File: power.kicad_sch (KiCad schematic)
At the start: 41 parts, among them U2 BQ25176J, U3 TPS61201DRC, U4 BQ51050BRHL

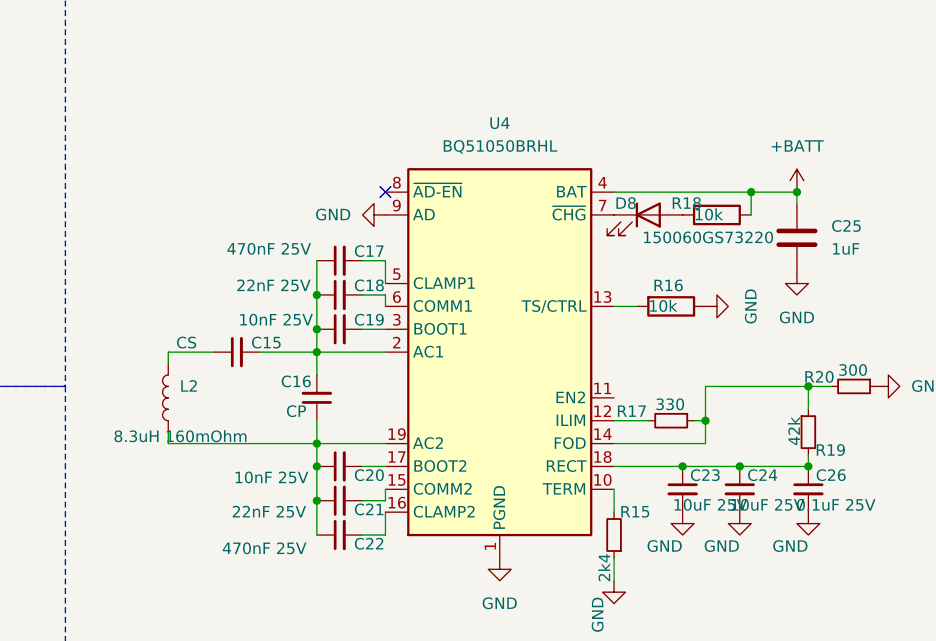
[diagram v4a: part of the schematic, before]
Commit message: start reshuffeling for qi-charge version
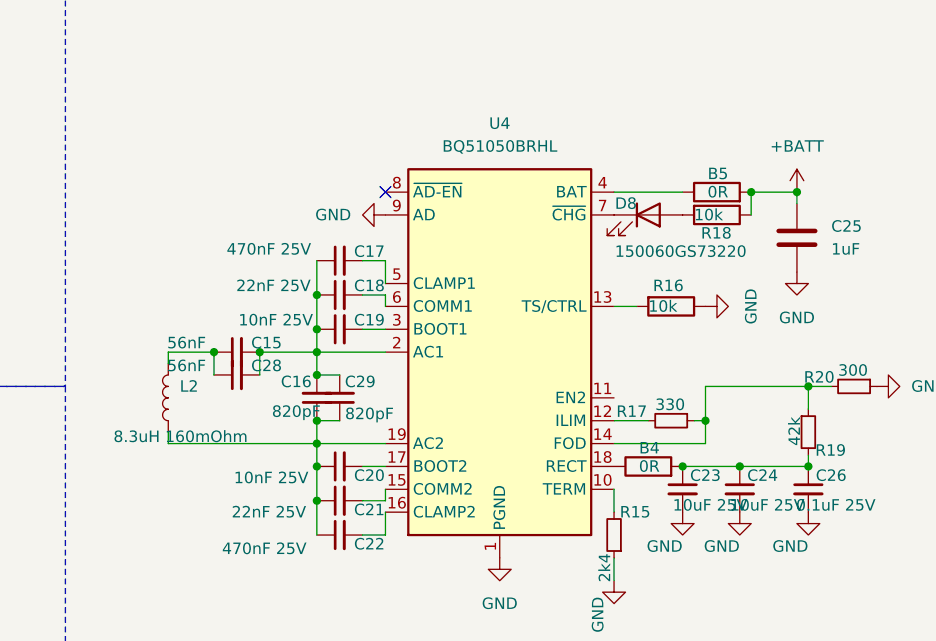
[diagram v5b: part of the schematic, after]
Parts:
- added B4, B5: 0R, Resistor_SMD:R_1206_3216Metric, symbol Device:R
- added C28: 56nF, Capacitor_SMD:C_0402_1005Metric, symbol Device:C_Small
- added C29: 820pF, Capacitor_SMD:C_0402_1005Metric, symbol Device:C_Small
- C15: value CS -> 56nF
- C16: value CP -> 820pF
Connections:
- net +BATT: now also B5.2; no longer U4.4 (BAT)
- net at C16.1, C20.1, C21.1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: now also C29.1
- net at C15.2, C16.2, C17.1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: now also C28.2, C29.2
- net at C23.1, C24.1, C26.1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: now also B4.2; no longer U4.18 (RECT)
- net at C15.1, L2.2: now also C28.1
- new net: B4.1, U4.18 (RECT)
- new net: B5.1, U4.4 (BAT)

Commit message: further work
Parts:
- C13: footprint Capacitor_SMD:C_0805_2012Metric -> Capacitor_SMD:C_0603_1608Metric
- R10, R11, R12, R13, R14, R16, R18, R8, R9: footprint Resistor_SMD:R_0805_2012Metric -> Resistor_SMD:R_0603_1608Metric
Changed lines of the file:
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@@
 			)
 		)
-		(property "Footprint" "Resistor_SMD:R_0805_2012Metric"
+		(property "Footprint" "Resistor_SMD:R_0603_1608Metric"
 			(at 218.44 68.072 90)
 			(effects
@@
 			)
 		)
-		(property "Footprint" "Resistor_SMD:R_0805_2012Metric"
+		(property "Footprint" "Resistor_SMD:R_0603_1608Metric"
 			(at 65.532 62.23 90)
 			(effects
@@
 			)
 		)
-		(property "Footprint" "Capacitor_SMD:C_0805_2012Metric"
+		(property "Footprint" "Capacitor_SMD:C_0603_1608Metric"
 			(at 107.6452 76.2 0)
 			(effects
@@
 			)
 		)
-		(property "Footprint" "Resistor_SMD:R_0805_2012Metric"
+		(property "Footprint" "Resistor_SMD:R_0603_1608Metric"
 			(at 86.36 129.032 90)
 			(effects
@@
 			)
 		)
-		(property "Footprint" "Resistor_SMD:R_0805_2012Metric"
+		(property "Footprint" "Resistor_SMD:R_0603_1608Metric"
 			(at 42.672 134.62 90)
 			(effects
@@
 			)
 		)
-		(property "Footprint" "Resistor_SMD:R_0805_2012Metric"
+		(property "Footprint" "Resistor_SMD:R_0603_1608Metric"
 			(at 79.248 140.97 90)
 			(effects
@@
 			)
 		)
-		(property "Footprint" "Resistor_SMD:R_0805_2012Metric"
+		(property "Footprint" "Resistor_SMD:R_0603_1608Metric"
 			(at 86.36 123.952 90)
 			(effects
@@
 			)
 		)
-		(property "Footprint" "Resistor_SMD:R_0805_2012Metric"
+		(property "Footprint" "Resistor_SMD:R_0603_1608Metric"
 			(at 213.36 78.232 90)
 			(effects
@@
 			)
 		)
-		(property "Footprint" "Resistor_SMD:R_0805_2012Metric"
+		(property "Footprint" "Resistor_SMD:R_0603_1608Metric"
 			(at 49.022 138.43 90)
 			(effects
@@
 			)
 		)
-		(property "Footprint" "Resistor_SMD:R_0805_2012Metric"
+		(property "Footprint" "Resistor_SMD:R_0603_1608Metric"
 			(at 65.532 76.2 90)
 			(effects

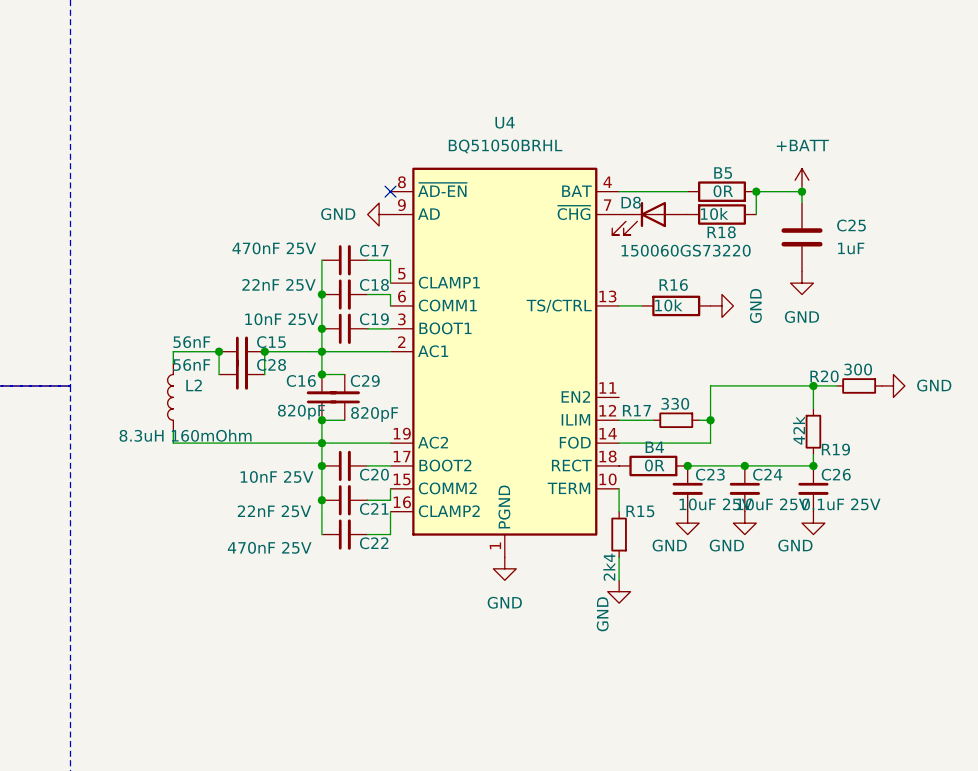
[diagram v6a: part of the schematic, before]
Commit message: add usb c connector
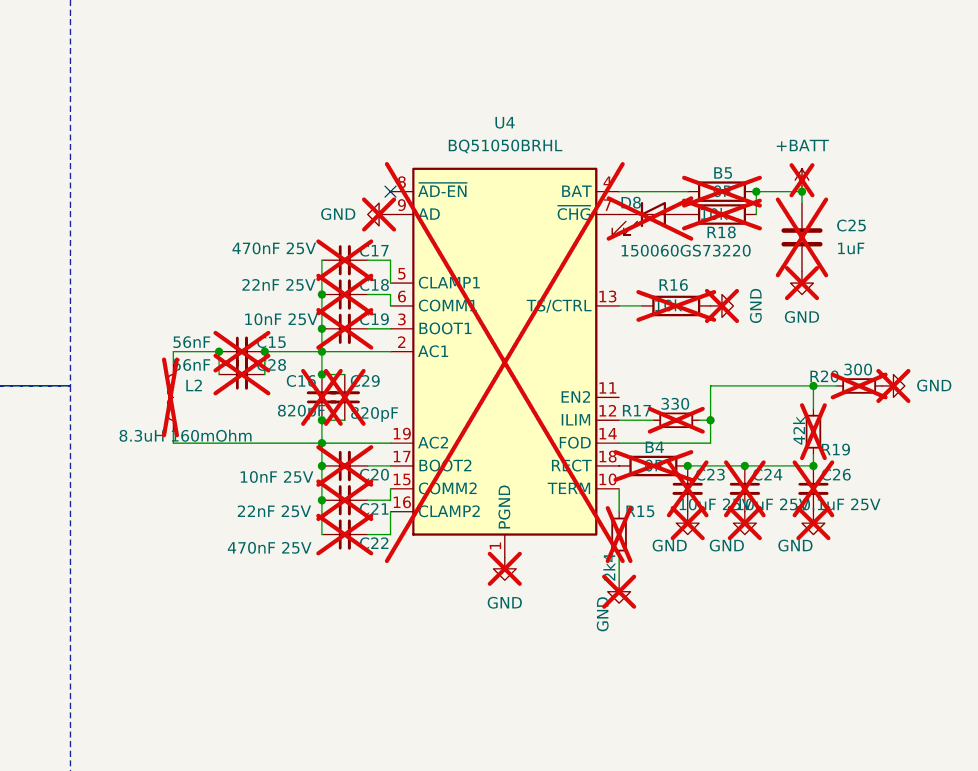
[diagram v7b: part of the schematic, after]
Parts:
- B4, B5, C15, C16, C17, C18, C19, C20, C21, C22, C23, C24, C25, C26, C28, C29, D8, L2, R15, R16, R17, R18, R19, R20, U4: now not fitted; now left out of the parts list
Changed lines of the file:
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@@
 		(unit 1)
 		(exclude_from_sim no)
-		(in_bom yes)
-		(on_board yes)
-		(dnp no)
+		(in_bom no)
+		(on_board no)
+		(dnp yes)
 		(property "Reference" "R18"
 			(at 216.662 71.882 90)
@@
 		(unit 1)
 		(exclude_from_sim no)
-		(in_bom yes)
-		(on_board yes)
-		(dnp no)
+		(in_bom no)
+		(on_board no)
+		(dnp yes)
 		(fields_autoplaced yes)
 		(property "Reference" "#PWR062"
@@
 		(unit 1)
 		(exclude_from_sim no)
-		(in_bom yes)
-		(on_board yes)
-		(dnp no)
+		(in_bom no)
+		(on_board no)
+		(dnp yes)
 		(property "Reference" "B4"
 			(at 212.09 95.758 90)
@@
 		(unit 1)
 		(exclude_from_sim no)
-		(in_bom yes)
-		(on_board yes)
-		(dnp no)
+		(in_bom no)
+		(on_board no)
+		(dnp yes)
 		(fields_autoplaced yes)
 		(property "Reference" "#PWR058"
@@
 		(unit 1)
 		(exclude_from_sim no)
-		(in_bom yes)
-		(on_board yes)
-		(dnp no)
+		(in_bom no)
+		(on_board no)
+		(dnp yes)
 		(property "Reference" "#PWR056"
 			(at 207.01 116.84 0)
@@
 		(unit 1)
 		(exclude_from_sim no)
-		(in_bom yes)
-		(on_board yes)
-		(dnp no)
+		(in_bom no)
+		(on_board no)
+		(dnp yes)
 		(property "Reference" "C21"
 			(at 179.832 102.616 90)
@@
 		(unit 1)
 		(exclude_from_sim no)
-		(in_bom yes)
-		(on_board yes)
-		(dnp no)
+		(in_bom no)
+		(on_board no)
+		(dnp yes)
 		(property "Reference" "C18"
 			(at 179.832 77.724 90)
@@
 		(unit 1)
 		(exclude_from_sim no)
-		(in_bom yes)
-		(on_board yes)
-		(dnp no)
+		(in_bom no)
+		(on_board no)
+		(dnp yes)
 		(property "Reference" "C19"
 			(at 179.832 81.534 90)
@@
 		(unit 1)
 		(exclude_from_sim no)
-		(in_bom yes)
-		(on_board yes)
-		(dnp no)
+		(in_bom no)
+		(on_board no)
+		(dnp yes)
 		(property "Reference" "C23"
 			(at 217.17 98.806 0)
@@
 		(unit 1)
 		(exclude_from_sim no)
-		(in_bom yes)
-		(on_board yes)
-		(dnp no)
+		(in_bom no)
+		(on_board no)
+		(dnp yes)
 		(property "Reference" "R15"
 			(at 211.074 102.87 0)
@@
 		(unit 1)
 		(exclude_from_sim no)
-		(in_bom yes)
-		(on_board yes)
-		(dnp no)
+		(in_bom no)
+		(on_board no)
+		(dnp yes)
 		(fields_autoplaced yes)
 		(property "Reference" "#PWR055"
@@
 		(unit 1)
 		(exclude_from_sim no)
-		(in_bom yes)
-		(on_board yes)
-		(dnp no)
+		(in_bom no)
+		(on_board no)
+		(dnp yes)
 		(property "Reference" "C24"
 			(at 223.52 98.806 0)
@@
 		(unit 1)
 		(exclude_from_sim no)
-		(in_bom yes)
-		(on_board yes)
-		(dnp no)
+		(in_bom no)
+		(on_board no)
+		(dnp yes)
 		(property "Reference" "C16"
 			(at 171.704 88.392 0)
@@
 		(unit 1)
 		(exclude_from_sim no)
-		(in_bom yes)
-		(on_board yes)
-		(dnp no)
+		(in_bom no)
+		(on_board no)
+		(dnp yes)
 		(property "Reference" "D8"
 			(at 209.55 68.58 0)
@@
 		(unit 1)
 		(exclude_from_sim no)
-		(in_bom yes)
-		(on_board yes)
-		(dnp no)
+		(in_bom no)
+		(on_board no)
+		(dnp yes)
 		(fields_autoplaced yes)
 		(property "Reference" "#PWR070"
@@
 		(unit 1)
 		(exclude_from_sim no)
-		(in_bom yes)
-		(on_board yes)
-		(dnp no)
+		(in_bom no)
+		(on_board no)
+		(dnp yes)
 		(property "Reference" "C15"
 			(at 168.402 84.074 90)
@@
 		(unit 1)
 		(exclude_from_sim no)
-		(in_bom yes)
-		(on_board yes)
-		(dnp no)
+		(in_bom no)
+		(on_board no)
+		(dnp yes)
 		(property "Reference" "C28"
 			(at 168.402 86.614 90)
@@
 		(unit 1)
 		(exclude_from_sim no)
-		(in_bom yes)
-		(on_board yes)
-		(dnp no)
+		(in_bom no)
+		(on_board no)
+		(dnp yes)
 		(property "Reference" "B5"
 			(at 219.71 65.278 90)
@@
 		(unit 1)
 		(exclude_from_sim no)
-		(in_bom yes)
-		(on_board yes)
-		(dnp no)
+		(in_bom no)
+		(on_board no)
+		(dnp yes)
 		(property "Reference" "C22"
 			(at 179.832 106.426 90)
@@
 		(unit 1)
 		(exclude_from_sim no)
-		(in_bom yes)
-		(on_board yes)
-		(dnp no)
+		(in_bom no)
+		(on_board no)
+		(dnp yes)
 		(property "Reference" "#PWR061"
 			(at 228.6 109.22 0)
@@
 		(unit 1)
 		(exclude_from_sim no)
-		(in_bom yes)
-		(on_board yes)
-		(dnp no)
+		(in_bom no)
+		(on_board no)
+		(dnp yes)
 		(property "Reference" "#PWR059"
 			(at 220.98 109.22 0)
@@
 		(unit 1)
 		(exclude_from_sim no)
-		(in_bom yes)
-		(on_board yes)
-		(dnp no)
+		(in_bom no)
+		(on_board no)
+		(dnp yes)
 		(fields_autoplaced yes)
 		(property "Reference" "C25"
@@
 		(unit 1)
 		(exclude_from_sim no)
-		(in_bom yes)
-		(on_board yes)
-		(dnp no)
+		(in_bom no)
+		(on_board no)
+		(dnp yes)
 		(property "Reference" "C26"
 			(at 231.14 98.806 0)
@@
 		(unit 1)
 		(exclude_from_sim no)
-		(in_bom yes)
-		(on_board yes)
-		(dnp no)
+		(in_bom no)
+		(on_board no)
+		(dnp yes)
 		(property "Reference" "C17"
 			(at 179.832 73.914 90)
@@
 		(unit 1)
 		(exclude_from_sim no)
-		(in_bom yes)
-		(on_board yes)
-		(dnp no)
+		(in_bom no)
+		(on_board no)
+		(dnp yes)
 		(property "Reference" "#PWR057"
 			(at 214.63 109.22 0)
@@
 		(unit 1)
 		(exclude_from_sim no)
-		(in_bom yes)
-		(on_board yes)
-		(dnp no)
+		(in_bom no)
+		(on_board no)
+		(dnp yes)
 		(property "Reference" "C20"
 			(at 179.832 98.806 90)
@@
 		(unit 1)
 		(exclude_from_sim no)
-		(in_bom yes)
-		(on_board yes)
-		(dnp no)
+		(in_bom no)
+		(on_board no)
+		(dnp yes)
 		(property "Reference" "R16"
 			(at 211.328 77.724 90)
@@
 		(unit 1)
 		(exclude_from_sim no)
-		(in_bom yes)
-		(on_board yes)
-		(dnp no)
+		(in_bom no)
+		(on_board no)
+		(dnp yes)
 		(property "Reference" "L2"
 			(at 158.75 88.8999 0)
@@
 		(unit 1)
 		(exclude_from_sim no)
-		(in_bom yes)
-		(on_board yes)
-		(dnp no)
+		(in_bom no)
+		(on_board no)
+		(dnp yes)
 		(property "Reference" "C29"
 			(at 178.816 88.392 0)
@@
 		(unit 1)
 		(exclude_from_sim no)
-		(in_bom yes)
-		(on_board yes)
-		(dnp no)
+		(in_bom no)
+		(on_board no)
+		(dnp yes)
 		(property "Reference" "R19"
 			(at 229.362 96.012 0)
@@
 		(unit 1)
 		(exclude_from_sim no)
-		(in_bom yes)
-		(on_board yes)
-		(dnp no)
+		(in_bom no)
+		(on_board no)
+		(dnp yes)
 		(property "Reference" "R17"
 			(at 207.264 91.694 90)
@@
 		(unit 1)
 		(exclude_from_sim no)
-		(in_bom yes)
-		(on_board yes)
-		(dnp no)
+		(in_bom no)
+		(on_board no)
+		(dnp yes)
 		(fields_autoplaced yes)
 		(property "Reference" "U4"
@@
 		(unit 1)
 		(exclude_from_sim no)
-		(in_bom yes)
-		(on_board yes)
-		(dnp no)
+		(in_bom no)
+		(on_board no)
+		(dnp yes)
 		(property "Reference" "R20"
 			(at 228.092 87.884 90)
@@
 		(unit 1)
 		(exclude_from_sim no)
-		(in_bom yes)
-		(on_board yes)
-		(dnp no)
+		(in_bom no)
+		(on_board no)
+		(dnp yes)
 		(fields_autoplaced yes)
 		(property "Reference" "#PWR054"
@@
 		(unit 1)
 		(exclude_from_sim no)
-		(in_bom yes)
-		(on_board yes)
-		(dnp no)
+		(in_bom no)
+		(on_board no)
+		(dnp yes)
 		(fields_autoplaced yes)
 		(property "Reference" "#PWR060"

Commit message: replace some components for JLC order
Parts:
- C11: mpn CL21A106KPFNNNF -> CL21B105KAFNNNG
- D6: mpn 150060BS73220 -> XL-1608UBC-04
- D7: mpn 150060GS73220 -> A-SP192DGHC-C01-4T
- R10: mpn CRCW080562K0FKEA -> (none)
- R11: mpn CRCW08054K99FKEA -> (none)
- R12, R13, R14: mpn CR0805-FX-1002ELF -> (none)
- R8: mpn CR0805-FX-6200ELF -> (none)
- R9: mpn CRCW080527K4FKEA -> (none)
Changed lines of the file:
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@@
 			)
 		)
-		(property "mpn" "150060BS73220"
+		(property "mpn" "XL-1608UBC-04"
 			(at 78.74 125.73 0)
 			(effects
@@
 			)
 		)
-		(property "mpn" "CRCW080562K0FKEA"
+		(property "mpn" ""
 			(at 67.31 62.23 0)
 			(effects
@@
 			)
 		)
-		(property "mpn" "CL21A106KPFNNNF"
+		(property "mpn" "CL21B105KAFNNNG "
 			(at 60.96 62.23 0)
 			(effects
@@
 			)
 		)
-		(property "mpn" "CR0805-FX-1002ELF "
+		(property "mpn" ""
 			(at 86.36 130.81 0)
 			(effects
@@
 			)
 		)
-		(property "mpn" "150060GS73220"
+		(property "mpn" "A-SP192DGHC-C01-4T"
 			(at 78.74 130.81 0)
 			(effects
@@
 			)
 		)
-		(property "mpn" "CR0805-FX-6200ELF "
+		(property "mpn" ""
 			(at 44.45 134.62 0)
 			(effects
@@
 			)
 		)
-		(property "mpn" "CR0805-FX-1002ELF "
+		(property "mpn" ""
 			(at 77.47 140.97 0)
 			(effects
@@
 			)
 		)
-		(property "mpn" "CR0805-FX-1002ELF "
+		(property "mpn" ""
 			(at 86.36 125.73 0)
 			(effects
@@
 			)
 		)
-		(property "mpn" "CRCW080527K4FKEA"
+		(property "mpn" ""
 			(at 50.8 138.43 0)
 			(effects
@@
 			)
 		)
-		(property "mpn" "CRCW08054K99FKEA"
+		(property "mpn" ""
 			(at 67.31 76.2 0)
 			(effects
